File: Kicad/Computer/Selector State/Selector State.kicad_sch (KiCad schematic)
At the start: 50 parts

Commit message: Added some LSF0102 pics.
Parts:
- removed IC?: SN74ALVC08PWR, SOP65P640X120-14N, symbol Texas_Instruments:SN74ALVC08PWR
- removed IC?: 74LVC595APW, SOIC127P600X175-16N, symbol Nexperia:74LVC595APW
- removed J? (x2): Conn_01x14_Male, Connector_PinHeader_2.54mm:PinHeader_1x14_P2.54mm_Vertical, symbol Connector:Conn_01x14_Male
- added C? (x3): C_Small, Capacitor_SMD:C_0805_2012Metric, symbol Device:C_Small
- added IC?: 74VHC595FT, SOP65P640X120-16N, symbol Toshiba:74VHC595FT
- added IC?: 74LVC2G08DP-Q100H, SOP65P400X110-8N, symbol Nexperia:74LVC2G08DP-Q100H
- added IC?: 74LVC4245APW,118, SOP65P640X110-24N, symbol Nexperia:74LVC4245APW,118
- added J1, J10, J12, J3, J4, J6, J7, J9: Conn_01x02_Male, Connector_PinHeader_2.54mm:PinHeader_1x02_P2.54mm_Vertical, symbol Connector:Conn_01x02_Male
- added J11, J8: Conn_01x10_Male, Connector_PinHeader_2.54mm:PinHeader_1x10_P2.54mm_Vertical, symbol Connector:Conn_01x10_Male
- added J2, J5: Conn_01x12_Male, Connector_PinHeader_2.54mm:PinHeader_1x12_P2.54mm_Vertical, symbol Connector:Conn_01x12_Male
- added NT4, NT5: NetTie_2, NetTie:NetTie-2_SMD_Pad0.5mm, symbol Device:NetTie_2
- added PS?: AP2210K-5.0TRG1, SOT95P282X130-5N, symbol Diodes_Inc:AP2210K-5.0TRG1
- gave numbers to parts that had none: 46
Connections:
- net Board ~{Reset}: now also IC?.3 (QD), J11.9 (Pin_9), J8.9 (Pin_9)
- net GND: now also IC10.13 (4I1), IC10.14 (4I0), IC10.15 (~{OE}), IC11.15 (~{OE}), C?.1, C?.1, C?.1, IC?.11 (GND), IC?.12 (GND), IC?.13 (GND), IC?.13 (~{G}), IC?.2 (DIR), IC?.22 (~{OE}), IC?.4 (GND), IC?.8 (GND), J1.1 (Pin_1), J10.1 (Pin_1), J12.1 (Pin_1), J3.1 (Pin_1), J4.1 (Pin_1), J6.1 (Pin_1), J7.1 (Pin_1), J9.1 (Pin_1), PS?.2 (GND)
- net MPU Lock-in: now also IC10.1 (S), IC11.1 (S), J2.9 (Pin_9), J5.9 (Pin_9)
- net PHI2 ~{Reset}: now also IC?.15 (QA), IC?.2 (1B)
- net Source 5V: now also R1.2, C?.2, J3.2 (Pin_2), J6.2 (Pin_2), PS?.1 (VIN), PS?.3 (EN)
- net VCC: now also C?.2, IC?.1 (VCC(A)), IC?.16 (VCC), IC?.23 (VCC(B)), IC?.24 (VCC(B)), IC?.8 (VCC), NT4.1, PS?.5 (VOUT); no longer R1.2
- net ~{Bank Latch}: now also IC?.10 (A7), J11.1 (Pin_1), J8.1 (Pin_1); no longer IC8.2 (1Y)
- net ~{Clock Enable}: now also J2.10 (Pin_10), J5.10 (Pin_10)
- net ~{Data Transmit}: now also IC?.9 (A6), J11.2 (Pin_2), J8.2 (Pin_2); no longer IC9.3 (1Y)
- net ~{Device Strobe}: now also IC?.6 (A3), J11.5 (Pin_5), J8.5 (Pin_5); no longer NT3.2
- net ~{PHI2}: now also IC?.3 (A0), J11.8 (Pin_8), J8.8 (Pin_8)
- net ~{PHI2} Naked: now also IC?.1 (1A)
- net ~{Power Error}: now also J11.10 (Pin_10), J8.10 (Pin_10)
- net ~{Read Bank Remap}: now also IC?.8 (A5), J11.3 (Pin_3), J8.3 (Pin_3); no longer NT1.2
- net ~{Reset}: now also IC?.10 (~{SCLR}), IC?.14 (SI), J2.11 (Pin_11), J5.11 (Pin_11)
- net ~{Select 0}: now also IC?.5 (2A), J2.1 (Pin_1), J5.1 (Pin_1)
- net ~{Select 1}: now also J2.2 (Pin_2), J5.2 (Pin_2)
- net ~{Select 2}: now also J2.3 (Pin_3), J5.3 (Pin_3)
- net ~{Select 3}: now also IC?.11 (SCK), IC?.12 (RCK), J2.4 (Pin_4), J5.4 (Pin_4)
- net ~{Select 4}: now also IC?.6 (2B), J2.5 (Pin_5), J5.5 (Pin_5), NT5.1
- net ~{Select 5}: now also J2.6 (Pin_6), J5.6 (Pin_6)
- net ~{Select 6}: now also J2.7 (Pin_7), J5.7 (Pin_7)
- net ~{Select 7}: now also J2.8 (Pin_8), J5.8 (Pin_8)
- net ~{Stop Selector}: now also IC?.7 (A4), J11.4 (Pin_4), J8.4 (Pin_4); no longer NT2.2
- net ~{Read Bank Remap}_{2}: now reaches IC10.10 (3I1)
- net ~{Read Bank Remap}_{2}: now also NT4.2
- net ~{Read Bank Remap}_{1}: now reaches IC10.11 (3I0)
- net ~{Read Bank Remap}_{1}: now also NT1.2
- net ~{Bank Latch}_{1}: now reaches IC10.2 (1I0)
- net ~{Bank Latch}_{1}: now also IC8.2 (1Y)
- net ~{Bank Latch}_{2}: now reaches IC10.3 (1I1)
- net ~{Bank Latch}_{2}: now also IC10.6 (2I1), IC8.4 (2Y)
- net at IC10.4 (1Y): now also IC?.14 (B7)
- net ~{Data Transmit}_{1}: now reaches IC10.5 (2I0)
- net ~{Data Transmit}_{1}: now also IC9.3 (1Y)
- net at IC10.7 (2Y): now also IC?.15 (B6)
- net at IC10.9 (3Y): now also IC?.16 (B5)
- net Read Selector_{2}: now reaches IC8.3 (2A)
- net Read Selector_{2}: now also IC11.10 (3I1), IC11.13 (4I1), IC11.6 (2I1), IC?.3 (2Y)
- net Read Selector_{1}: now reaches IC11.11 (3I0)
- net Read Selector_{1}: now also IC9.8 (3Y)
- net at IC11.12 (4Y): now also IC?.21 (B0)
- net ~{PHI2}_{1}: now reaches IC11.14 (4I0)
- net ~{PHI2}_{1}: now also IC?.7 (1Y)
- net ~{Device Strobe}_{1}: now reaches IC11.2 (1I0)
- net ~{Device Strobe}_{1}: now also NT3.2
- net ~{Device Strobe}_{2}: now reaches IC11.3 (1I1)
- net ~{Device Strobe}_{2}: now also NT5.2
- net at IC11.4 (1Y): now also IC?.18 (B3)
- net Write Selector_{1}: now reaches IC11.5 (2I0)
- net Write Selector_{1}: now also IC9.6 (2Y)
- net at IC11.7 (2Y): now also IC?.19 (B2)
- net at IC11.9 (3Y): now also IC?.20 (B1)
- new net: C?.2, PS?.4 (BYP)
- new net: J1.2 (Pin_2), J4.2 (Pin_2)
- new net: J12.2 (Pin_2), J9.2 (Pin_2)
- new net: J2.12 (Pin_12), J5.12 (Pin_12)
- new net: J10.2 (Pin_2), J7.2 (Pin_2)
- new net: IC?.17 (B4), NT2.2
- new net Read Selector: IC?.4 (A1), J11.7 (Pin_7), J8.7 (Pin_7)
- new net Write Selector: IC?.5 (A2), J11.6 (Pin_6), J8.6 (Pin_6)
- no-connect marks 17 -> 20
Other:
- note added: "Connectors"
- note added: "Power"
- moved on the sheet: IC10, IC11, IC8, IC9, NT1, NT2, NT3, NT6

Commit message: Began routing Selector.
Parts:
- removed C? (x3): C_Small, Capacitor_SMD:C_0805_2012Metric, symbol Device:C_Small
- removed LED4: 150224VS73100A, 150224VS73100A, symbol Wurth_Elektronik:150224VS73100A
- removed RN1: CAY16-681J4LF, SamacSys_Parts:CAY16-J4, symbol Bourns:CAY16-681J4LF
- added C15, C16, C17: C_Small, Capacitor_SMD:C_0805_2012Metric, symbol Device:C_Small
- added NT7: NetTie_2, NetTie:NetTie-2_SMD_Pad0.5mm, symbol Device:NetTie_2
- added RN1: CAY16-472J4LF, CAY16472J4LF, symbol Bourns:CAY16-472J4LF
- added RN5, RN6: CAY16-470J4LF, CAY16470J4LF, symbol Bourns:CAY16-470J4LF
- IC1: Arrow Part Number FAN2558S38X -> (none); Arrow Price/Stock https://www.arrow.com/en/products/fan2558s38x/on-semiconduc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 -> (none); Silkscreen (none) -> FAN2558S
- gave numbers to parts that had none: 4
- renumbered LED10 to LD10, LED11 to LD11, LED12 to LD12, LD1 to LD13, LD2 to LD14
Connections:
- net Board ~{Reset}: now also IC6.4 (A3)
- net GND: now also C15.1, C16.1, C17.1, RN1.5 (R4), RN1.7 (R2), RN1.8 (R1); no longer RN4.3 (R3)
- net MPU Lock-in: now also IC6.3 (A2)
- net Read Selector: now also IC7.8 (A7), RN6.6 (R3); no longer IC12.4 (A1)
- net Reset LED: now also NT7.2
- net Source 5V: now also C2.2
- net Write Selector: now also IC7.7 (A6), RN6.7 (R2); no longer IC12.5 (A2)
- net ~{Bank Latch}: now also IC7.2 (A1), RN5.8 (R1); no longer IC12.10 (A7)
- net ~{Clock Enable}: now also IC6.2 (A1)
- net ~{Data Transmit}: now also IC7.3 (A2), RN5.7 (R2); no longer IC12.9 (A6)
- net ~{Device Strobe}: now also IC7.6 (A5), RN6.8 (R1); no longer IC12.6 (A3)
- net ~{PHI2}: now also IC7.9 (A8), RN6.5 (R4); no longer IC12.3 (A0)
- net ~{Read Bank Remap}: now also IC7.4 (A3), RN5.6 (R3); no longer IC12.8 (A5)
- net ~{Reset}: now also NT7.1
- net ~{Stop Selector}: now also IC7.5 (A4), RN5.5 (R4); no longer IC12.7 (A4)
- net at PS1.4 (BYP): now also C3.2
- net at LED1.1: now also RN1.1 (R1)
- net Select 2 ^{AND} Enable: now reaches IC2.8 (3Y), IC9.2 (1B), NT1.1
- net Select 1 ^{AND} Enable: now reaches IC2.6 (2Y), IC8.1 (1A), IC9.1 (1A)
- net Select 4 ^{AND} Enable: now reaches IC3.3 (1Y), NT3.1
- net at LED2.1: now also RN1.2 (R2)
- net at LED3.1: now also RN1.4 (R4)
- net Select 7 ^{AND} Enable: now reaches IC3.11 (4Y), IC9.10 (3B)
- net Select 5 ^{AND} Enable: now reaches IC3.6 (2Y), IC9.4 (2A), IC9.9 (3A)
- net Select 6 ^{AND} Enable: now reaches IC3.8 (3Y), IC9.5 (2B)
- net at RN4.5 (R4): now also LD14.1
- net at RN4.6 (R3): no longer LD14.1
- net Select 3 ^{AND} Enable: now reaches IC2.11 (4Y)
- net VCC renamed 3V
- net 3V: now also C15.2, C16.2, C17.2; no longer C10.2, C2.2, C3.2, C4.2, C5.2, C6.2, C8.2, C9.2, IC12.1 (VCC(A)), IC4.16 (VCC), IC6.1 (DIR), IC6.20 (VCC), IC7.1 (DIR), IC7.20 (VCC), NT6.1, PS1.5 (VOUT)
- new net: IC12.6 (A3), RN6.1 (R1)
- new net: IC12.5 (A2), RN6.2 (R2)
- new net: IC12.4 (A1), RN6.3 (R3)
- new net: IC12.3 (A0), RN6.4 (R4)
- new net: IC12.10 (A7), RN5.1 (R1)
- new net: IC12.9 (A6), RN5.2 (R2)
- new net: IC12.8 (A5), RN5.3 (R3)
- new net: IC12.7 (A4), RN5.4 (R4)
- new net 5V: C10.2, C4.2, C5.2, C6.2, C8.2, C9.2, IC12.1 (5V), IC4.16 (5V), IC6.1 (DIR), IC6.20 (5V), IC7.1 (DIR), IC7.20 (5V), NT6.1, PS1.5 (VOUT)
- no-connect marks 20 -> 30
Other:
- note added: "LED Display"
- moved on the sheet: C5, C6, IC1, IC12, IC6, IC7, J4, J5, J6, J7, J8, J9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

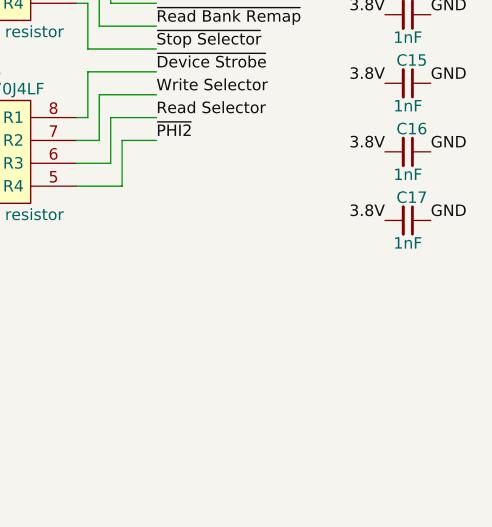
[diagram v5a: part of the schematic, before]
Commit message: Routed most Selector signals.
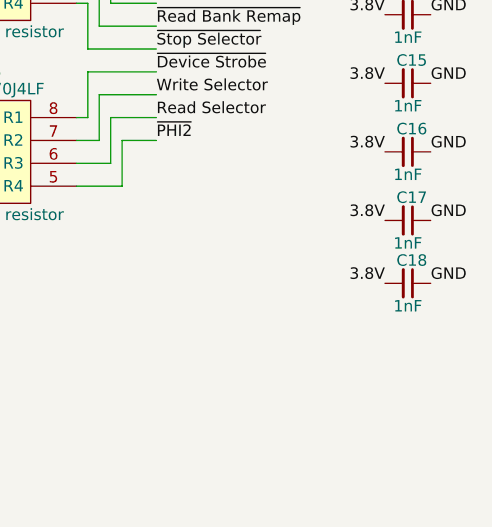
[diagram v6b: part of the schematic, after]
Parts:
- added C18: C_Small, Capacitor_SMD:C_0805_2012Metric, symbol Device:C_Small
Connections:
- net 3V: now also C18.2
- net GND: now also C18.1
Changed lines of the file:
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@@
     (effects (font (size 1.27 1.27)) (justify left bottom))
+  )
+  (label "3.8V" (at 364.49 189.865 180)
+    (effects (font (size 1.27 1.27)) (justify right bottom))
   )
   (label "~{Data Transmit}_{2}" (at 182.88 191.77 0)
@@
   (label "~{Data Transmit}_{2}" (at 228.6 149.86 180)
     (effects (font (size 1.27 1.27)) (justify right bottom))
+  )
+  (label "GND" (at 369.57 189.865 0)
+    (effects (font (size 1.27 1.27)) (justify left bottom))
   )
   (label "GND" (at 35.56 186.69 180)
@@
       (effects (font (size 1.27 1.27)) hide)
     )
+    (pin "1")
+    (pin "2")
+  )
+  (symbol (lib_id "Device:C_Small") (at 367.03 189.865 270) (unit 1)
+    (in_bom yes) (on_board yes)
+    (property "Reference" "C18" (id 0) (at 365.76 187.325 90)
+      (effects (font (size 1.27 1.27)) (justify left))
+    )
+    (property "Value" "C_Small" (id 1) (at 364.998 190.119 0)
+      (effects (font (size 1.27 1.27)) (justify left) hide)
+    )
+    (property "Footprint" "Capacitor_SMD:C_0805_2012Metric" (id 2) (at 367.03 189.865 0)
+      (effects (font (size 1.27 1.27)) hide)
+    )
+    (property "Datasheet" "~" (id 3) (at 367.03 189.865 0)
+      (effects (font (size 1.27 1.27)) hide)
+    )
+    (property "Description" "1nF" (id 4) (at 367.03 192.405 90))
     (pin "1")
     (pin "2")
@@
       (reference "C17") (unit 1) (value "C_Small") (footprint "Capacitor_SMD:C_0805_2012Metric")
     )
+    (path "/6a52c2ad-8926-4d15-a36a-715cd93189b4"
+      (reference "C18") (unit 1) (value "C_Small") (footprint "Capacitor_SMD:C_0805_2012Metric")
+    )
     (path "/585313b9-631f-4f6d-9c00-aa1b6482ae61"

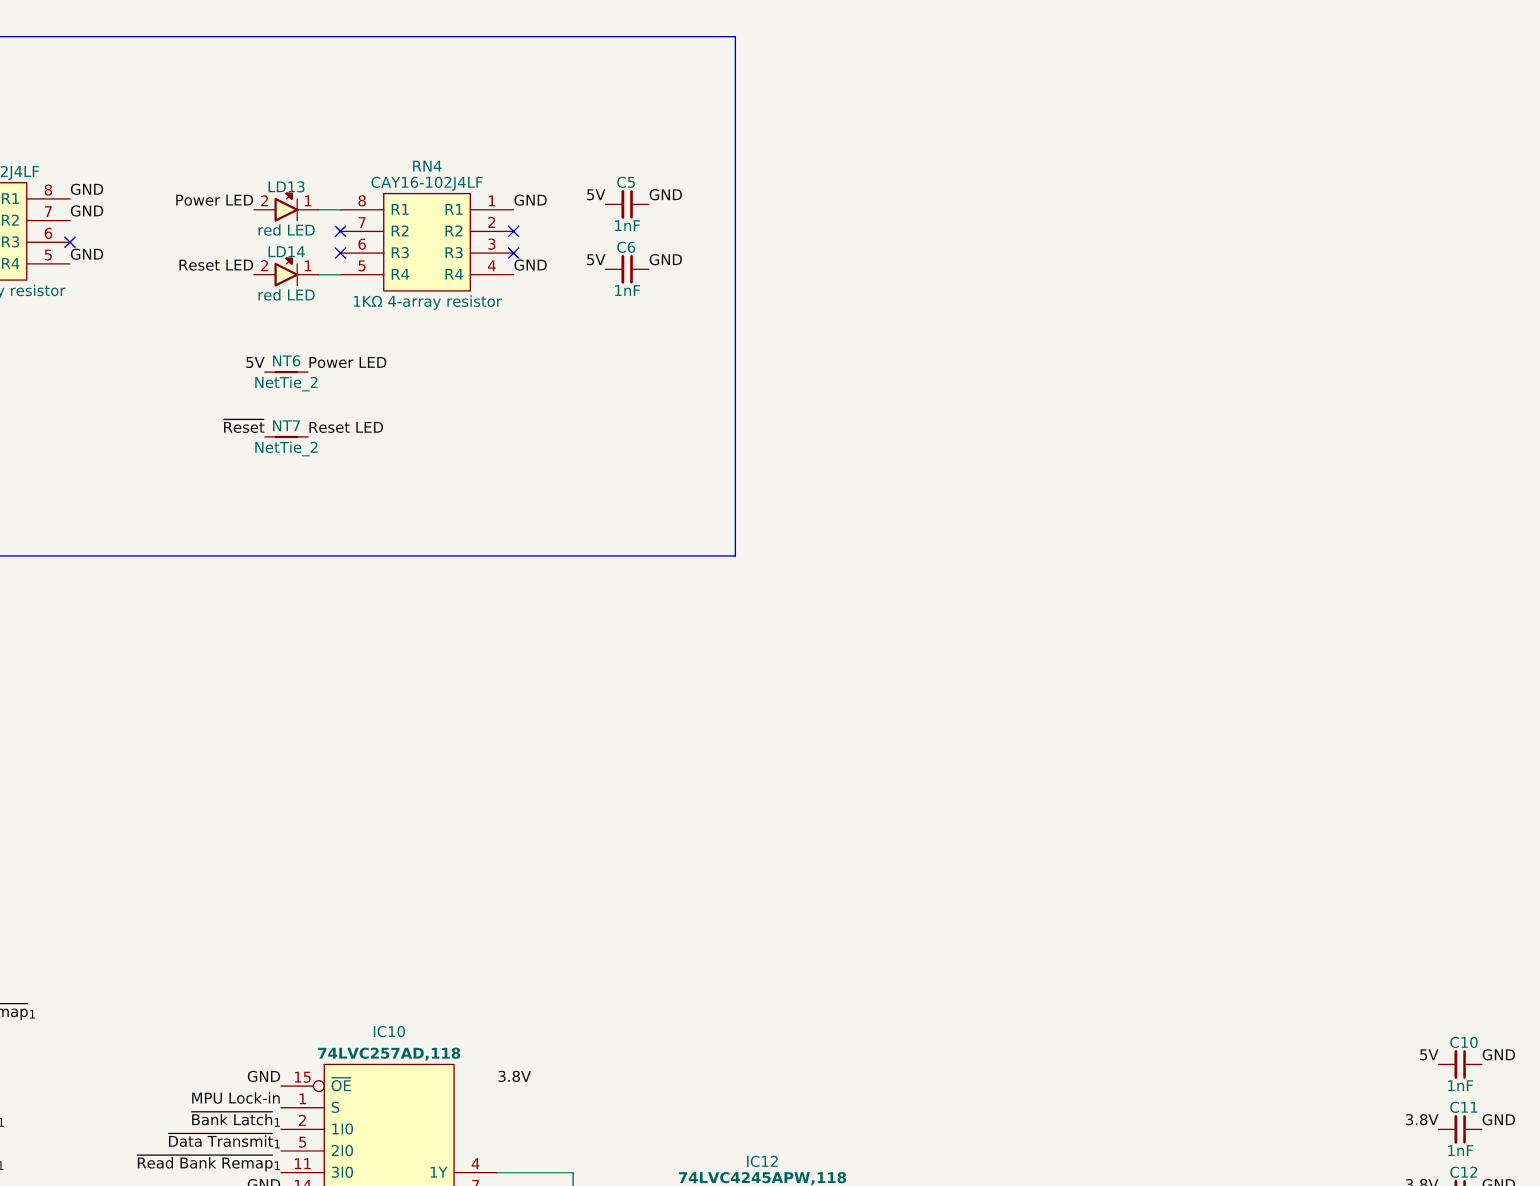
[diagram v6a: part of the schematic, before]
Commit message: Finished routing Selector Clock.
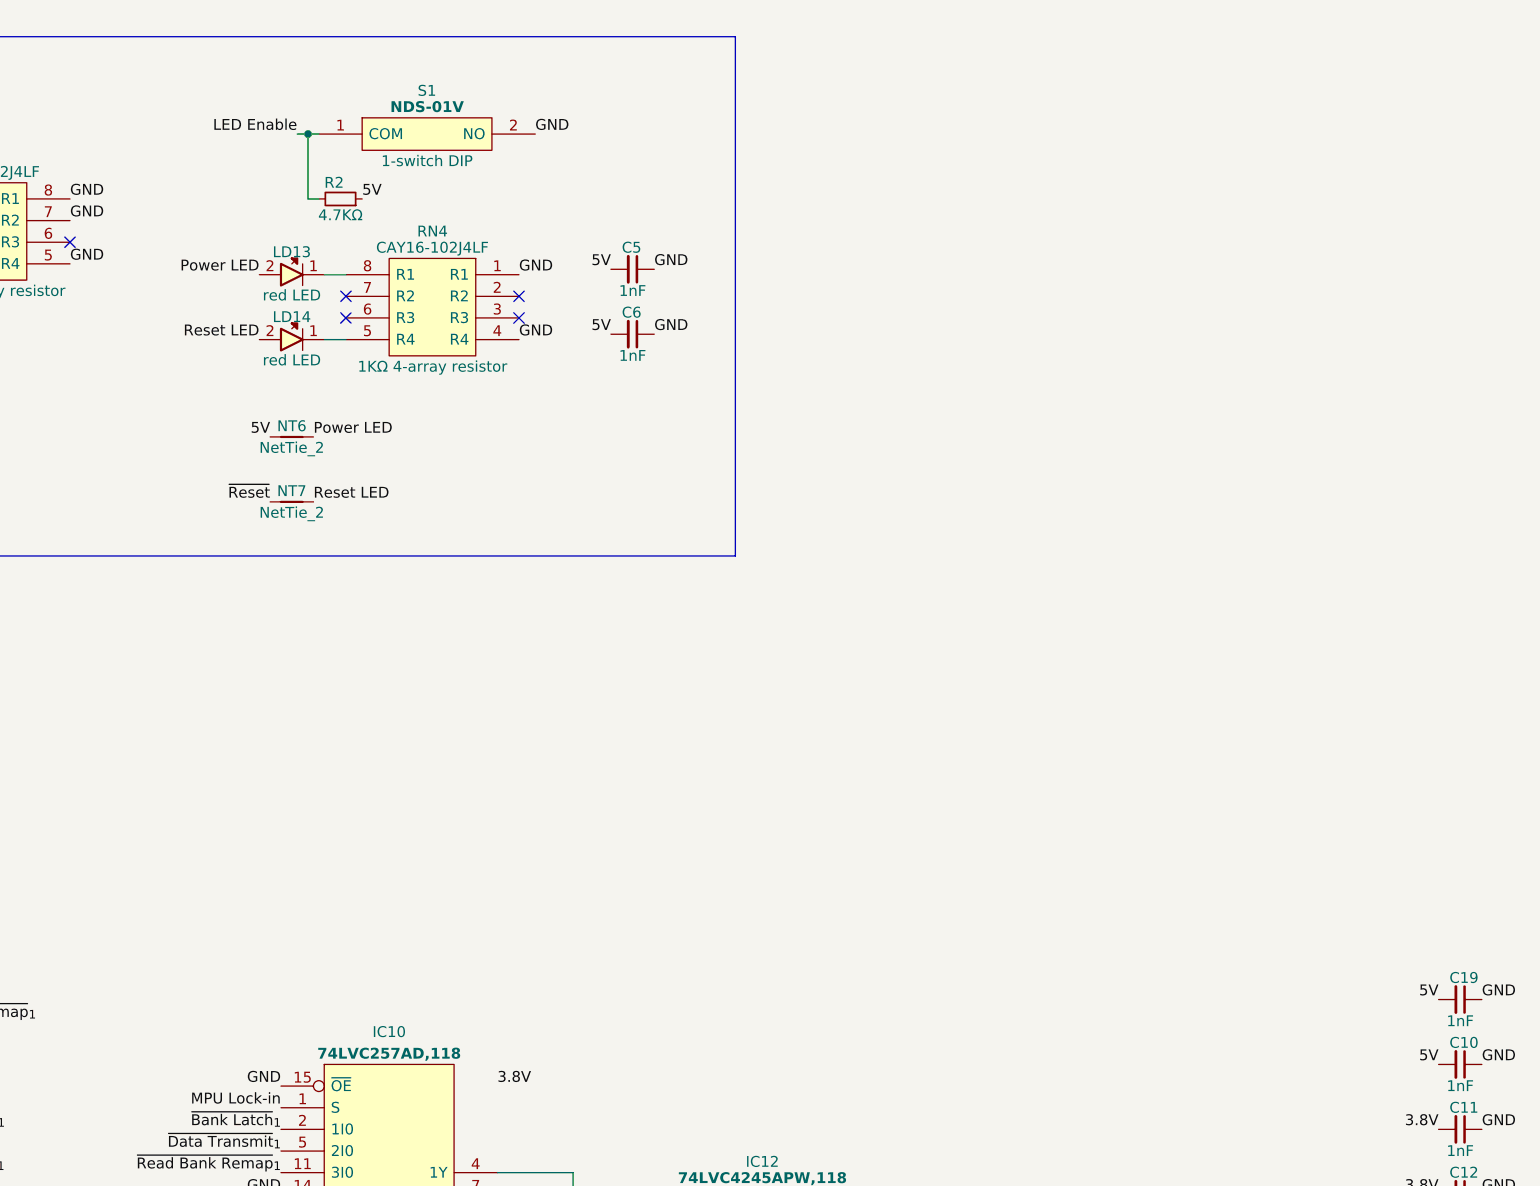
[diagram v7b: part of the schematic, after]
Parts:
- added C19: C_Small, Capacitor_SMD:C_0805_2012Metric, symbol Device:C_Small
- added R2: R_Small, Resistor_SMD:R_0805_2012Metric, symbol Device:R_Small
- added S1: NDS-01V, NDS01V, symbol Apem:NDS-01V
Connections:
- net 5V: now also C19.2, R2.1
- net GND: now also C19.1, S1.2 (NO)
- net LED Enable: now also R2.2, S1.1 (COM)
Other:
- moved on the sheet: C5, C6, LD13, LD14, NT6, NT7, RN4

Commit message: Re-routed Selector State based on new simulation.
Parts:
- removed C3: C_Small, Capacitor_SMD:C_0805_2012Metric, symbol Device:C_Small
- removed LD14: 150224SS73100, SamacSys_Parts:150224SS73100A, symbol Wurth_Elektronik:150224SS73100
- removed LED9: 150224VS73100A, 150224VS73100A, symbol Wurth_Elektronik:150224VS73100A
- removed PS1: AP2210K-5.0TRG1, SOT95P282X130-5N, symbol Diodes_Inc:AP2210K-5.0TRG1
- removed R1, R2: R_Small, Resistor_SMD:R_0805_2012Metric, symbol Device:R_Small
- removed RN1: CAY16-472J4LF, CAY16472J4LF, symbol Bourns:CAY16-472J4LF
- removed RN4: CAY16-102J4LF, SamacSys_Parts:CAY16-J4, symbol Bourns:CAY16-102J4LF
- added IC13: MCP1802T-5002I_OT, SOT95P270X145-5N, symbol Microchip:MCP1802T-5002I_OT
- added LED4: 150224VS73100A, 150224VS73100A, symbol Wurth_Elektronik:150224VS73100A
- added NT8, NT9: NetTie_2, NetTie:NetTie-2_SMD_Pad0.5mm, symbol Device:NetTie_2
- added R2, R3: R_0805, SamacSys_Parts:R_0805, symbol HCP65:R_0805
- added RN1: CAY16-681J4LF, SamacSys_Parts:CAY16-J4, symbol Bourns:CAY16-681J4LF
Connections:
- net 5V: now also IC13.5 (VOUT), R2.2
- net Board ~{Reset}: now also IC4.1 (QB); no longer IC4.3 (QD)
- net GND: now also IC11.2 (1I0), IC11.3 (1I1), IC12.18 (B3), IC7.6 (A5), IC8.11 (5A), IC8.13 (6A), IC8.5 (3A), IC8.9 (4A), IC13.2 (VSS), R3.2, RN1.5 (R4), RN1.6 (R3), RN1.7 (R2), RN1.8 (R1); no longer RN3.8 (R1)
- net LED Enable: now also R2.1
- net Read Selector_{2}: now also NT8.2; no longer IC11.13 (4I1), IC11.6 (2I1), IC5.3 (2Y), IC8.3 (2A)
- net Source 5V: now also IC13.1 (VIN), IC13.3 (~{SHDN})
- net ~{Bank Latch}_{2}: now also NT3.2; no longer IC10.6 (2I1), IC8.4 (2Y)
- net ~{Reset}: no longer NT7.1
- net ~{Select 4}: no longer NT5.1
- net Write Selector^{LED}: now reaches IC7.13 (B6), LD10.2
- net at LED1.1: now also RN1.1 (R1)
- net ~{Clock Enable}^{LED}: now reaches IC6.18 (B1), LED1.2
- net at J1.2 (Pin_2): no longer J4.2 (Pin_2)
- net at J12.2 (Pin_2): no longer J9.2 (Pin_2)
- net at J5.12 (Pin_12): no longer J2.12 (Pin_12)
- net MPU ~{Reset}: now reaches IC4.2 (QC)
- net MPU ~{Reset}: now also IC6.5 (A4), J11.5 (Pin_5), J8.5 (Pin_5)
- net ~{Data Transmit}^{LED}: now reaches IC7.17 (B2), LED6.2
- net ~{Stop Selector}^{LED}: now reaches IC7.15 (B4), LED8.2
- net ~{PHI2}^{LED}: now reaches IC7.11 (B8), LD12.2
- net Read Selector^{LED}: now reaches IC7.12 (B7), LD11.2
- net ~{Read Bank Remap}^{LED}: now reaches IC7.16 (B3), LED7.2
- net ~{Bank Latch}^{LED}: now reaches IC7.18 (B1), LED5.2
- net at LD13.1: now also R3.1
- net at RN6.1 (R1): no longer IC12.6 (A3)
- net at J10.2 (Pin_2): no longer J7.2 (Pin_2)
- net at IC11.4 (1Y): no longer IC12.18 (B3)
- net MPU ~{Reset}^{LED}: now reaches IC6.15 (B4)
- net MPU ~{Reset}^{LED}: now also LED4.2
- net Board ~{Reset}^{LED}: now reaches IC6.16 (B3), LED3.2
- net MPU Lock-in^{LED}: now reaches IC6.17 (B2), LED2.2
- net at LED2.1: now also RN1.2 (R2)
- net at LED3.1: now also RN1.3 (R3)
- net 3V renamed 3.8V
- net Power LED renamed Power^{LED}
- net Reset LED renamed Write Selector_{2}
- net Write Selector_{2}: now also IC11.6 (2I1)
- net Select 3 ^{AND} Enable: no longer names the net of IC2.11 (4Y)
- net Select 4 ^{AND} Enable: no longer names the net of NT3.1
- net Select 4 ^{AND} Enable: now also IC8.4 (2Y), NT5.1; no longer IC3.3 (1Y)
- removed net ~{Device Strobe}: IC7.6 (A5), J11.5 (Pin_5), J8.5 (Pin_5), RN6.8 (R1)
- removed net ~{Device Strobe}_{1}: IC11.2 (1I0), NT3.2
- net ~{Device Strobe}_{2} renamed ~{Data Transmit}_{2}
- net ~{Data Transmit}_{2}: now also IC10.6 (2I1); no longer IC11.3 (1I1)
- removed net ~{Power Error}: IC1.4 (PG), J11.10 (Pin_10), J8.10 (Pin_10)
- new net: IC5.3 (2Y), IC8.3 (2A), NT7.1, NT8.1, NT9.1
- new net: LED4.1, RN1.4 (R4)
- new net ~{PHI2}_{2}: IC11.13 (4I1), NT9.2
- no-connect marks 30 -> 40
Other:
- moved on the sheet: C7, C8, C9, IC12, LED5, NT4, RN2, RN3
